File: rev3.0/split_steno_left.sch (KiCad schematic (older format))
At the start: 33 parts, among them J1 USB_B, J2 Audio-Jack-4, P1 TC2030-IDC, SW1 SW_Push, SW10 SW_Push, SW11 SW_Push, SW12 SW_Push, SW13 SW_Push, SW14 SW_Push, SW15 SW_Push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

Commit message: finished routing
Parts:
- added J3: Conn_02x04_Odd_Even, Pin_Headers:Pin_Header_Straight_2x04_Pitch2.54mm, symbol Conn_02x04_Odd_Even
- added J4, J5: Conn_01x03, Pin_Headers:Pin_Header_Straight_1x03_Pitch2.54mm, symbol Conn_01x03
- added J6: Conn_01x02, Pin_Headers:Pin_Header_Straight_1x02_Pitch2.54mm, symbol Conn_01x02
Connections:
- net GND: now also J3.1 (Pin_1), J4.3 (Pin_3), J5.3 (Pin_3), J6.2 (Pin_2)
- net KEY1: now also U2.24 (PD4/OC1A/~SS~)
- net KEY10: now also U2.43 (AC3/ADC3/PA3)
- net KEY11: now also U2.11 (SCLIN/SCL/XCK0/OC0AHS/OC0B/PC1)
- net KEY12: now also U2.10 (SDAIN/SDA/~OC0ALS~/OC0A/PC0)
- net KEY13: now also U2.3 (AC0OUT/AC7/ADC7/PA7)
- net KEY14: now also U2.2 (AC1OUT/AC6/ADC6/PA6)
- net KEY15: now also U2.44 (AC4/ADC4/PA4)
- net KEY16: now also SW19.1, U2.5 (ADC9/PB1)
- net KEY17: now also SW20.1, U2.4 (AREFB/ADC8/PB0); no longer SW19.1
- net KEY18: now also U2.1 (AC5/ADC5/PA5); no longer SW20.1
- net KEY2: now also U2.25 (PD5/OC1B/XCK1/MOSI)
- net KEY3: now also U2.33 (PE3/OC0D/TXD0)
- net KEY4: now also U2.36 (PR0/XTAL2/TOSC2)
- net KEY5: now also U2.42 (AC2/ADC2/PA2)
- net KEY6: now also U2.23 (PD3/OC0D/TXD0)
- net KEY7: now also U2.20 (PD0/OC0A)
- net KEY8: now also U2.32 (PE2/OC0C/RXD0)
- net KEY9: now also U2.41 (AC1/ADC1/PA1)
- net VCC: now also J3.2 (Pin_2), J4.1 (Pin_1), J5.1 (Pin_1)
- net CE: now reaches U2.12 (SDAOUT/RXD0/~OC0BLS~/OC0C/PC2)
- net CE: now also J3.3 (Pin_3)
- net IRQ: now reaches U2.13 (SCLOUT/TXD0/OC0BHS/OC0D/PC3)
- net IRQ: now also J3.8 (Pin_8)
- net CSN: now reaches U2.14 (~SS~/~OC0CLS~/OC1A/PC4)
- net CSN: now also J3.4 (Pin_4)
- net MOSI: now reaches U2.15 (MOSI/XCK1/OC0CHS/OC1B/PC5)
- net MOSI: now also J3.6 (Pin_6)
- net MISO: now reaches U2.16 (CLKRTC/MISO/RXD1/~OC0DLS~/PC6)
- net MISO: now also J3.7 (Pin_7)
- net SCK: now reaches U2.17 (CLKOUT/SCK/TXD1/OC0DHS/PC7)
- net SCK: now also J3.5 (Pin_5)
- net EXTRA1: now reaches U2.22 (PD2/OC0C/RXD0)
- net EXTRA1: now also J5.2 (Pin_2)
- net EXTRA2: now reaches U2.37 (PR1/XTAL1/TOSC1)
- net EXTRA2: now also J6.1 (Pin_1)
- net UNDER_RGB: now reaches U2.6 (DAC0/ADC10/PB2)
- net UNDER_RGB: now also J4.2 (Pin_2)
- no-connect marks 3 -> 6
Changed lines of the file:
@@
 $EndComp
 Text Label 6250 1675 2    60   ~ 0
-KEY17
+KEY16
 $Comp
 L SW_Push SW20
@@
 $EndComp
 Text Label 6250 1900 2    60   ~ 0
-KEY18
+KEY17
 $Comp
 L SW_Push SW1
@@
 	-1   0    0    1
 $EndComp
+$Comp
+L VCC #PWR020
+U 1 1 5AFFE474
+P 7400 2725
+F 0 "#PWR020" H 7400 2575 50  0001 C CNN
+F 1 "VCC" H 7400 2875 50  0000 C CNN
+F 2 "" H 7400 2725 50  0001 C CNN
+F 3 "" H 7400 2725 50  0001 C CNN
+	1    7400 2725
+	1    0    0    -1
+$EndComp
+$Comp
+L VCC #PWR021
+U 1 1 5AFFE4E2
+P 7075 3225
+F 0 "#PWR021" H 7075 3075 50  0001 C CNN
+F 1 "VCC" H 7075 3375 50  0000 C CNN
+F 2 "" H 7075 3225 50  0001 C CNN
+F 3 "" H 7075 3225 50  0001 C CNN
+	1    7075 3225
+	0    1    1    0
+$EndComp
+$Comp
+L Conn_02x04_Odd_Even J3
+U 1 1 5B14A652
+P 5500 2850
+F 0 "J3" H 5550 3050 50  0000 C CNN
+F 1 "Conn_02x04_Odd_Even" H 5550 2550 50  0000 C CNN
+F 2 "Pin_Headers:Pin_Header_Straight_2x04_Pitch2.54mm" H 5500 2850 50  0001 C CNN
+F 3 "" H 5500 2850 50  0001 C CNN
+	1    5500 2850
+	1    0    0    -1
+$EndComp
+Text Label 9775 3775 0    60   ~ 0
+IRQ
+Text Label 9775 3675 0    60   ~ 0
+CE
+Text Label 9775 3875 0    60   ~ 0
+CSN
+Text Label 9775 3975 0    60   ~ 0
+MOSI
+Text Label 9775 4075 0    60   ~ 0
+MISO
+Text Label 9775 4175 0    60   ~ 0
+SCK
 Wire Wire Line
 	8475 1875 8875 1875
@@
 Connection ~ 7400 3025
 Connection ~ 7225 3125
-$Comp
-L VCC #PWR020
-U 1 1 5AFFE474
-P 7400 2725
-F 0 "#PWR020" H 7400 2575 50  0001 C CNN
-F 1 "VCC" H 7400 2875 50  0000 C CNN
-F 2 "" H 7400 2725 50  0001 C CNN
-F 3 "" H 7400 2725 50  0001 C CNN
-	1    7400 2725
-	1    0    0    -1
-$EndComp
-$Comp
-L VCC #PWR021
-U 1 1 5AFFE4E2
-P 7075 3225
-F 0 "#PWR021" H 7075 3075 50  0001 C CNN
-F 1 "VCC" H 7075 3375 50  0000 C CNN
-F 2 "" H 7075 3225 50  0001 C CNN
-F 3 "" H 7075 3225 50  0001 C CNN
-	1    7075 3225
+Wire Wire Line
+	6625 3425 6675 3425
+Wire Wire Line
+	7225 2825 7225 2725
+Wire Wire Line
+	7225 2725 7400 2725
+Text Label 5300 2950 2    60   ~ 0
+SCK
+Text Label 5300 3050 2    60   ~ 0
+MISO
+Text Label 5300 2850 2    60   ~ 0
+CE
+Text Label 5800 2850 0    60   ~ 0
+CSN
+Text Label 5800 2950 0    60   ~ 0
+MOSI
+Text Label 5800 3050 0    60   ~ 0
+IRQ
+$Comp
+L GND #PWR022
+U 1 1 5B14B3CA
+P 5300 2750
+F 0 "#PWR022" H 5300 2500 50  0001 C CNN
+F 1 "GND" H 5300 2600 50  0000 C CNN
+F 2 "" H 5300 2750 50  0001 C CNN
+F 3 "" H 5300 2750 50  0001 C CNN
+	1    5300 2750
+	-1   0    0    1
+$EndComp
+$Comp
+L VCC #PWR023
+U 1 1 5B14B797
+P 5800 2750
+F 0 "#PWR023" H 5800 2600 50  0001 C CNN
+F 1 "VCC" H 5800 2900 50  0000 C CNN
+F 2 "" H 5800 2750 50  0001 C CNN
+F 3 "" H 5800 2750 50  0001 C CNN
+	1    5800 2750
+	1    0    0    -1
+$EndComp
+Text Label 9775 3575 0    60   ~ 0
+KEY11
+Text Label 9775 3475 0    60   ~ 0
+KEY12
+Text Label 9775 2575 0    60   ~ 0
+KEY15
+Text Label 9775 2775 0    60   ~ 0
+KEY14
+Text Label 9775 2875 0    60   ~ 0
+KEY13
+Text Label 9775 2675 0    60   ~ 0
+KEY18
+Text Label 9775 3025 0    60   ~ 0
+KEY17
+Text Label 9775 3125 0    60   ~ 0
+KEY16
+Text Label 9775 3225 0    60   ~ 0
+UNDER_RGB
+Text Label 5775 3525 2    60   ~ 0
+UNDER_RGB
+Text Label 7975 3475 2    60   ~ 0
+KEY7
+Text Label 7975 3775 2    60   ~ 0
+KEY6
+Text Label 7975 3875 2    60   ~ 0
+KEY1
+Text Label 7975 3975 2    60   ~ 0
+KEY2
+Text Label 7975 3325 2    60   ~ 0
+KEY3
+Text Label 7975 2775 2    60   ~ 0
+KEY4
+Text Label 7975 3225 2    60   ~ 0
+KEY8
+Text Label 9775 2275 0    60   ~ 0
+KEY9
+Text Label 9775 2375 0    60   ~ 0
+KEY5
+Text Label 9775 2475 0    60   ~ 0
+KEY10
+Text Label 7975 2875 2    60   ~ 0
+EXTRA2
+Text Label 7975 3675 2    60   ~ 0
+EXTRA1
+NoConn ~ 7975 3575
+NoConn ~ 9775 2175
+NoConn ~ 9775 3325
+Text Label 5775 4100 2    60   ~ 0
+EXTRA1
+Text Label 5775 4500 2    60   ~ 0
+EXTRA2
+$Comp
+L Conn_01x03 J4
+U 1 1 5B15D849
+P 5975 3525
+F 0 "J4" H 5975 3725 50  0000 C CNN
+F 1 "Conn_01x03" H 5975 3325 50  0000 C CNN
+F 2 "Pin_Headers:Pin_Header_Straight_1x03_Pitch2.54mm" H 5975 3525 50  0001 C CNN
+F 3 "" H 5975 3525 50  0001 C CNN
+	1    5975 3525
+	1    0    0    -1
+$EndComp
+$Comp
+L VCC #PWR024
+U 1 1 5B15DA49
+P 5775 3425
+F 0 "#PWR024" H 5775 3275 50  0001 C CNN
+F 1 "VCC" H 5775 3575 50  0000 C CNN
+F 2 "" H 5775 3425 50  0001 C CNN
+F 3 "" H 5775 3425 50  0001 C CNN
+	1    5775 3425
+	1    0    0    -1
+$EndComp
+$Comp
+L GND #PWR025
+U 1 1 5B15DAC3
+P 5775 3625
+F 0 "#PWR025" H 5775 3375 50  0001 C CNN
+F 1 "GND" H 5775 3475 50  0000 C CNN
+F 2 "" H 5775 3625 50  0001 C CNN
+F 3 "" H 5775 3625 50  0001 C CNN
+	1    5775 3625
 	0    1    1    0
 $EndComp
-Wire Wire Line
-	6625 3425 6675 3425
-Wire Wire Line
-	7225 2825 7225 2725
-Wire Wire Line
-	7225 2725 7400 2725
+$Comp
+L Conn_01x03 J5
+U 1 1 5B15DE45
+P 5975 4100
+F 0 "J5" H 5975 4300 50  0000 C CNN
+F 1 "Conn_01x03" H 5975 3900 50  0000 C CNN
+F 2 "Pin_Headers:Pin_Header_Straight_1x03_Pitch2.54mm" H 5975 4100 50  0001 C CNN
+F 3 "" H 5975 4100 50  0001 C CNN
+	1    5975 4100
+	1    0    0    -1
+$EndComp
+$Comp
+L VCC #PWR026
+U 1 1 5B15E01D
+P 5775 4000
+F 0 "#PWR026" H 5775 3850 50  0001 C CNN
+F 1 "VCC" H 5775 4150 50  0000 C CNN
+F 2 "" H 5775 4000 50  0001 C CNN
+F 3 "" H 5775 4000 50  0001 C CNN
+	1    5775 4000
+	1    0    0    -1
+$EndComp
+$Comp
+L GND #PWR027
+U 1 1 5B15E097
+P 5775 4200
+F 0 "#PWR027" H 5775 3950 50  0001 C CNN
+F 1 "GND" H 5775 4050 50  0000 C CNN
+F 2 "" H 5775 4200 50  0001 C CNN
+F 3 "" H 5775 4200 50  0001 C CNN
+	1    5775 4200
+	0    1    1    0
+$EndComp
+$Comp
+L Conn_01x02 J6
+U 1 1 5B15E1F9
+P 5975 4500
+F 0 "J6" H 5975 4600 50  0000 C CNN
+F 1 "Conn_01x02" H 5975 4300 50  0000 C CNN
+F 2 "Pin_Headers:Pin_Header_Straight_1x02_Pitch2.54mm" H 5975 4500 50  0001 C CNN
+F 3 "" H 5975 4500 50  0001 C CNN
+	1    5975 4500
+	1    0    0    -1
+$EndComp
+$Comp
+L GND #PWR028
+U 1 1 5B15E563
+P 5775 4600
+F 0 "#PWR028" H 5775 4350 50  0001 C CNN
+F 1 "GND" H 5775 4450 50  0000 C CNN
+F 2 "" H 5775 4600 50  0001 C CNN
+F 3 "" H 5775 4600 50  0001 C CNN
+	1    5775 4600
+	0    1    1    0
+$EndComp
 $EndSCHEMATC

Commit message: library managed
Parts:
- C1, C2, C3, C4, C5: footprint Capacitors_SMD:C_0603_HandSoldering -> lib_fp:C_0603_HandSoldering
- F1: footprint Fuse_Holders_and_Fuses:Fuse_SMD1206_HandSoldering -> lib_fp:Fuse_SMD1206_HandSoldering
- J1: footprint keyboard_parts:USB_miniB_hirose_5S8 -> lib_fp:USB_miniB_hirose_5S8
- J2: footprint Keebio-Parts:TRRS-PJ-320A -> lib_fp:TRRS-PJ-320A
- J3: footprint Pin_Headers:Pin_Header_Straight_2x04_Pitch2.54mm -> lib_fp:Pin_Header_Straight_2x04_Pitch2.54mm
- J4, J5: footprint Pin_Headers:Pin_Header_Straight_1x03_Pitch2.54mm -> lib_fp:Pin_Header_Straight_1x03_Pitch2.54mm
- J6: footprint Pin_Headers:Pin_Header_Straight_1x02_Pitch2.54mm -> lib_fp:Pin_Header_Straight_1x02_Pitch2.54mm
- P1: footprint Tag-Connect:TC2030-NL_SMALL_AND_IDC_PDI -> lib_fp:TC2030-NL_SMALL_AND_IDC_PDI
- R1, R2: footprint Resistors_SMD:R_0603_HandSoldering -> lib_fp:R_0603_HandSoldering
- SW1, SW10, SW11, SW12, SW13, SW14, SW15, SW16, SW17, SW18, SW2, SW3, SW4, SW5, SW6, SW7, SW8, SW9: footprint MX_Alps_Hybrid:MX-1U-NoLED -> lib_fp:MX-1U-NoLED
- SW19, SW20: footprint MX_Alps_Hybrid:MX-2U-NoLED -> lib_fp:MX-2U-NoLED
- U1: footprint TO_SOT_Packages_SMD:SOT-23-5_HandSoldering -> lib_fp:SOT-23-5_HandSoldering
- U2: footprint Housings_QFP:TQFP-44_10x10mm_Pitch0.8mm -> lib_fp:TQFP-44_10x10mm_Pitch0.8mm
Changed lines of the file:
@@
 F 0 "J1" H 6575 4525 50  0000 L CNN
 F 1 "USB_B" H 6575 4425 50  0000 L CNN
-F 2 "keyboard_parts:USB_miniB_hirose_5S8" H 6925 4025 50  0001 C CNN
+F 2 "lib_fp:USB_miniB_hirose_5S8" H 6925 4025 50  0001 C CNN
 F 3 "" H 6925 4025 50  0001 C CNN
 	1    6775 4075
@@
 F 0 "J2" H 6825 3105 50  0000 C CNN
 F 1 "Audio-Jack-4" H 6995 2655 50  0000 C CNN
-F 2 "Keebio-Parts:TRRS-PJ-320A" H 7125 3125 50  0001 C CNN
+F 2 "lib_fp:TRRS-PJ-320A" H 7125 3125 50  0001 C CNN
 F 3 "" H 7125 3125 50  0001 C CNN
 	1    6875 3025
@@
 F 0 "P1" H 9575 875 40  0000 L CNN
 F 1 "TC2030-IDC" H 9625 1275 40  0000 C CNN
-F 2 "Tag-Connect:TC2030-NL_SMALL_AND_IDC_PDI" H 9625 1075 60  0001 C CNN
+F 2 "lib_fp:TC2030-NL_SMALL_AND_IDC_PDI" H 9625 1075 60  0001 C CNN
 F 3 "" H 9625 1075 60  0001 C CNN
 	1    9625 1075
@@
 F 0 "U1" H 7725 1650 60  0000 C CNN
 F 1 "MIC550X" H 7925 1050 60  0000 C CNN
-F 2 "TO_SOT_Packages_SMD:SOT-23-5_HandSoldering" H 7925 1350 60  0001 C CNN
+F 2 "lib_fp:SOT-23-5_HandSoldering" H 7925 1350 60  0001 C CNN
 F 3 "" H 7925 1350 60  0001 C CNN
 	1    7925 1350
@@
 F 0 "U2" H 8125 4375 50  0000 L BNN
 F 1 "ATXMEGA-A4U-EPAD" H 9075 1925 50  0000 L BNN
-F 2 "Housings_QFP:TQFP-44_10x10mm_Pitch0.8mm" H 8875 3175 50  0001 C CIN
+F 2 "lib_fp:TQFP-44_10x10mm_Pitch0.8mm" H 8875 3175 50  0001 C CIN
 F 3 "" H 8875 3175 50  0001 C CNN
 	1    8875 3175
@@
 F 0 "C1" H 8525 1450 50  0000 L CNN
 F 1 "10uF" H 8525 1250 50  0000 L CNN
-F 2 "Capacitors_SMD:C_0603_HandSoldering" H 8538 1200 50  0001 C CNN
+F 2 "lib_fp:C_0603_HandSoldering" H 8538 1200 50  0001 C CNN
 F 3 "" H 8500 1350 50  0001 C CNN
 	1    8500 1350
@@
 F 0 "C2" H 9100 1725 50  0000 L CNN
 F 1 "0.1uF" H 9100 1525 50  0000 L CNN
-F 2 "Capacitors_SMD:C_0603_HandSoldering" H 9113 1475 50  0001 C CNN
+F 2 "lib_fp:C_0603_HandSoldering" H 9113 1475 50  0001 C CNN
 F 3 "" H 9075 1625 50  0001 C CNN
 	1    9075 1625
@@
 F 0 "C3" H 9350 1725 50  0000 L CNN
 F 1 "0.1uF" H 9350 1525 50  0000 L CNN
-F 2 "Capacitors_SMD:C_0603_HandSoldering" H 9363 1475 50  0001 C CNN
+F 2 "lib_fp:C_0603_HandSoldering" H 9363 1475 50  0001 C CNN
 F 3 "" H 9325 1625 50  0001 C CNN
 	1    9325 1625
@@
 F 0 "C4" H 9600 1725 50  0000 L CNN
 F 1 "0.1uF" H 9600 1525 50  0000 L CNN
-F 2 "Capacitors_SMD:C_0603_HandSoldering" H 9613 1475 50  0001 C CNN
+F 2 "lib_fp:C_0603_HandSoldering" H 9613 1475 50  0001 C CNN
 F 3 "" H 9575 1625 50  0001 C CNN
 	1    9575 1625
@@
 F 0 "C5" H 9850 1725 50  0000 L CNN
 F 1 "0.1uF" H 9850 1525 50  0000 L CNN
-F 2 "Capacitors_SMD:C_0603_HandSoldering" H 9863 1475 50  0001 C CNN
+F 2 "lib_fp:C_0603_HandSoldering" H 9863 1475 50  0001 C CNN
 F 3 "" H 9825 1625 50  0001 C CNN
 	1    9825 1625
@@
 F 0 "SW5" H 4275 1325 50  0000 L CNN
 F 1 "SW_Push" H 4225 1165 50  0001 C CNN
-F 2 "MX_Alps_Hybrid:MX-1U-NoLED" H 4225 1425 50  0001 C CNN
+F 2 "lib_fp:MX-1U-NoLED" H 4225 1425 50  0001 C CNN
 F 3 "" H 4225 1425 50  0001 C CNN
 	1    4225 1225
@@
 F 0 "F1" V 7305 3875 50  0000 C CNN
 F 1 "Fuse" V 7150 3875 50  0000 C CNN
-F 2 "Fuse_Holders_and_Fuses:Fuse_SMD1206_HandSoldering" V 7155 3875 50  0001 C CNN
+F 2 "lib_fp:Fuse_SMD1206_HandSoldering" V 7155 3875 50  0001 C CNN
 F 3 "" H 7225 3875 50  0001 C CNN
 	1    7225 3875
@@
 F 0 "SW6" H 4275 1550 50  0000 L CNN
 F 1 "SW_Push" H 4225 1390 50  0001 C CNN
-F 2 "MX_Alps_Hybrid:MX-1U-NoLED" H 4225 1650 50  0001 C CNN
+F 2 "lib_fp:MX-1U-NoLED" H 4225 1650 50  0001 C CNN
 F 3 "" H 4225 1650 50  0001 C CNN
 	1    4225 1450
@@
 F 0 "SW7" H 4275 1775 50  0000 L CNN
 F 1 "SW_Push" H 4225 1615 50  0001 C CNN
-F 2 "MX_Alps_Hybrid:MX-1U-NoLED" H 4225 1875 50  0001 C CNN
+F 2 "lib_fp:MX-1U-NoLED" H 4225 1875 50  0001 C CNN
 F 3 "" H 4225 1875 50  0001 C CNN
 	1    4225 1675
@@
 F 0 "SW8" H 4275 2000 50  0000 L CNN
 F 1 "SW_Push" H 4225 1840 50  0001 C CNN
-F 2 "MX_Alps_Hybrid:MX-1U-NoLED" H 4225 2100 50  0001 C CNN
+F 2 "lib_fp:MX-1U-NoLED" H 4225 2100 50  0001 C CNN
 F 3 "" H 4225 2100 50  0001 C CNN
 	1    4225 1900
@@
 F 0 "SW9" H 5025 1325 50  0000 L CNN
 F 1 "SW_Push" H 4975 1165 50  0001 C CNN
-F 2 "MX_Alps_Hybrid:MX-1U-NoLED" H 4975 1425 50  0001 C CNN
+F 2 "lib_fp:MX-1U-NoLED" H 4975 1425 50  0001 C CNN
 F 3 "" H 4975 1425 50  0001 C CNN
 	1    4975 1225
@@
 F 0 "SW10" H 5025 1550 50  0000 L CNN
 F 1 "SW_Push" H 4975 1390 50  0001 C CNN
-F 2 "MX_Alps_Hybrid:MX-1U-NoLED" H 4975 1650 50  0001 C CNN
+F 2 "lib_fp:MX-1U-NoLED" H 4975 1650 50  0001 C CNN
 F 3 "" H 4975 1650 50  0001 C CNN
 	1    4975 1450
@@
 F 0 "SW11" H 5025 1775 50  0000 L CNN
 F 1 "SW_Push" H 4975 1615 50  0001 C CNN
-F 2 "MX_Alps_Hybrid:MX-1U-NoLED" H 4975 1875 50  0001 C CNN
+F 2 "lib_fp:MX-1U-NoLED" H 4975 1875 50  0001 C CNN
 F 3 "" H 4975 1875 50  0001 C CNN
 	1    4975 1675
@@
 F 0 "SW12" H 5025 2000 50  0000 L CNN
 F 1 "SW_Push" H 4975 1840 50  0001 C CNN
-F 2 "MX_Alps_Hybrid:MX-1U-NoLED" H 4975 2100 50  0001 C CNN
+F 2 "lib_fp:MX-1U-NoLED" H 4975 2100 50  0001 C CNN
 F 3 "" H 4975 2100 50  0001 C CNN
 	1    4975 1900
@@
 F 0 "SW13" H 5750 1325 50  0000 L CNN
 F 1 "SW_Push" H 5700 1165 50  0001 C CNN
-F 2 "MX_Alps_Hybrid:MX-1U-NoLED" H 5700 1425 50  0001 C CNN
+F 2 "lib_fp:MX-1U-NoLED" H 5700 1425 50  0001 C CNN
 F 3 "" H 5700 1425 50  0001 C CNN
 	1    5700 1225
@@
 F 0 "SW14" H 5750 1550 50  0000 L CNN
 F 1 "SW_Push" H 5700 1390 50  0001 C CNN
-F 2 "MX_Alps_Hybrid:MX-1U-NoLED" H 5700 1650 50  0001 C CNN
+F 2 "lib_fp:MX-1U-NoLED" H 5700 1650 50  0001 C CNN
 F 3 "" H 5700 1650 50  0001 C CNN
 	1    5700 1450
@@
 F 0 "SW15" H 5750 1775 50  0000 L CNN
 F 1 "SW_Push" H 5700 1615 50  0001 C CNN
-F 2 "MX_Alps_Hybrid:MX-1U-NoLED" H 5700 1875 50  0001 C CNN
+F 2 "lib_fp:MX-1U-NoLED" H 5700 1875 50  0001 C CNN
 F 3 "" H 5700 1875 50  0001 C CNN
 	1    5700 1675
@@
 F 0 "SW16" H 5750 2000 50  0000 L CNN
 F 1 "SW_Push" H 5700 1840 50  0001 C CNN
-F 2 "MX_Alps_Hybrid:MX-1U-NoLED" H 5700 2100 50  0001 C CNN
+F 2 "lib_fp:MX-1U-NoLED" H 5700 2100 50  0001 C CNN
 F 3 "" H 5700 2100 50  0001 C CNN
 	1    5700 1900
@@
 F 0 "SW17" H 6500 1325 50  0000 L CNN
 F 1 "SW_Push" H 6450 1165 50  0001 C CNN
-F 2 "MX_Alps_Hybrid:MX-1U-NoLED" H 6450 1425 50  0001 C CNN
+F 2 "lib_fp:MX-1U-NoLED" H 6450 1425 50  0001 C CNN
 F 3 "" H 6450 1425 50  0001 C CNN
 	1    6450 1225
@@
 F 0 "SW18" H 6500 1550 50  0000 L CNN
 F 1 "SW_Push" H 6450 1390 50  0001 C CNN
-F 2 "MX_Alps_Hybrid:MX-1U-NoLED" H 6450 1650 50  0001 C CNN
+F 2 "lib_fp:MX-1U-NoLED" H 6450 1650 50  0001 C CNN
 F 3 "" H 6450 1650 50  0001 C CNN
 	1    6450 1450
@@
 F 0 "SW19" H 6500 1775 50  0000 L CNN
 F 1 "SW_Push" H 6450 1615 50  0001 C CNN
-F 2 "MX_Alps_Hybrid:MX-2U-NoLED" H 6450 1875 50  0001 C CNN
+F 2 "lib_fp:MX-2U-NoLED" H 6450 1875 50  0001 C CNN
 F 3 "" H 6450 1875 50  0001 C CNN
 	1    6450 1675
@@
 F 0 "SW20" H 6500 2000 50  0000 L CNN
 F 1 "SW_Push" H 6450 1840 50  0001 C CNN
-F 2 "MX_Alps_Hybrid:MX-2U-NoLED" H 6450 2100 50  0001 C CNN
+F 2 "lib_fp:MX-2U-NoLED" H 6450 2100 50  0001 C CNN
 F 3 "" H 6450 2100 50  0001 C CNN
 	1    6450 1900
@@
 F 0 "SW1" H 3550 1325 50  0000 L CNN
 F 1 "SW_Push" H 3500 1165 50  0001 C CNN
-F 2 "MX_Alps_Hybrid:MX-1U-NoLED" H 3500 1425 50  0001 C CNN
+F 2 "lib_fp:MX-1U-NoLED" H 3500 1425 50  0001 C CNN
 F 3 "" H 3500 1425 50  0001 C CNN
 	1    3500 1225
@@
 F 0 "SW2" H 3550 1550 50  0000 L CNN
 F 1 "SW_Push" H 3500 1390 50  0001 C CNN
-F 2 "MX_Alps_Hybrid:MX-1U-NoLED" H 3500 1650 50  0001 C CNN
+F 2 "lib_fp:MX-1U-NoLED" H 3500 1650 50  0001 C CNN
 F 3 "" H 3500 1650 50  0001 C CNN
 	1    3500 1450
@@
 F 0 "SW3" H 3550 1775 50  0000 L CNN
 F 1 "SW_Push" H 3500 1615 50  0001 C CNN
-F 2 "MX_Alps_Hybrid:MX-1U-NoLED" H 3500 1875 50  0001 C CNN
+F 2 "lib_fp:MX-1U-NoLED" H 3500 1875 50  0001 C CNN
 F 3 "" H 3500 1875 50  0001 C CNN
 	1    3500 1675
@@
 F 0 "SW4" H 3550 2000 50  0000 L CNN
 F 1 "SW_Push" H 3500 1840 50  0001 C CNN
-F 2 "MX_Alps_Hybrid:MX-1U-NoLED" H 3500 2100 50  0001 C CNN
+F 2 "lib_fp:MX-1U-NoLED" H 3500 2100 50  0001 C CNN
 F 3 "" H 3500 2100 50  0001 C CNN
 	1    3500 1900
@@
 F 0 "R1" V 7305 2975 50  0000 C CNN
 F 1 "4.7k" V 7225 2975 50  0000 C CNN
-F 2 "Resistors_SMD:R_0603_HandSoldering" V 7155 2975 50  0001 C CNN
+F 2 "lib_fp:R_0603_HandSoldering" V 7155 2975 50  0001 C CNN
 F 3 "" H 7225 2975 50  0001 C CNN
 	1    7225 2975
@@
 F 0 "R2" V 7480 2875 50  0000 C CNN
 F 1 "4.7k" V 7400 2875 50  0000 C CNN
-F 2 "Resistors_SMD:R_0603_HandSoldering" V 7330 2875 50  0001 C CNN
+F 2 "lib_fp:R_0603_HandSoldering" V 7330 2875 50  0001 C CNN
 F 3 "" H 7400 2875 50  0001 C CNN
 	1    7400 2875
@@
 F 0 "J3" H 5550 3050 50  0000 C CNN
 F 1 "Conn_02x04_Odd_Even" H 5550 2550 50  0000 C CNN
-F 2 "Pin_Headers:Pin_Header_Straight_2x04_Pitch2.54mm" H 5500 2850 50  0001 C CNN
+F 2 "lib_fp:Pin_Header_Straight_2x04_Pitch2.54mm" H 5500 2850 50  0001 C CNN
 F 3 "" H 5500 2850 50  0001 C CNN
 	1    5500 2850
@@
 F 0 "J4" H 5975 3725 50  0000 C CNN
 F 1 "Conn_01x03" H 5975 3325 50  0000 C CNN
-F 2 "Pin_Headers:Pin_Header_Straight_1x03_Pitch2.54mm" H 5975 3525 50  0001 C CNN
+F 2 "lib_fp:Pin_Header_Straight_1x03_Pitch2.54mm" H 5975 3525 50  0001 C CNN
 F 3 "" H 5975 3525 50  0001 C CNN
 	1    5975 3525
@@
 F 0 "J5" H 5975 4300 50  0000 C CNN
 F 1 "Conn_01x03" H 5975 3900 50  0000 C CNN
-F 2 "Pin_Headers:Pin_Header_Straight_1x03_Pitch2.54mm" H 5975 4100 50  0001 C CNN
+F 2 "lib_fp:Pin_Header_Straight_1x03_Pitch2.54mm" H 5975 4100 50  0001 C CNN
 F 3 "" H 5975 4100 50  0001 C CNN
 	1    5975 4100
@@
 F 0 "J6" H 5975 4600 50  0000 C CNN
 F 1 "Conn_01x02" H 5975 4300 50  0000 C CNN
-F 2 "Pin_Headers:Pin_Header_Straight_1x02_Pitch2.54mm" H 5975 4500 50  0001 C CNN
+F 2 "lib_fp:Pin_Header_Straight_1x02_Pitch2.54mm" H 5975 4500 50  0001 C CNN
 F 3 "" H 5975 4500 50  0001 C CNN
 	1    5975 4500

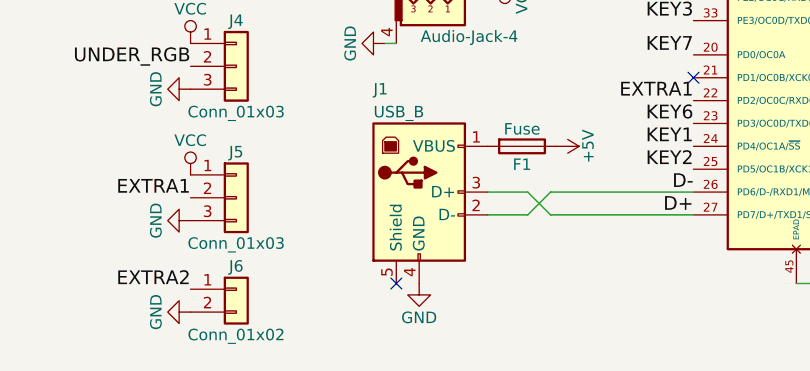
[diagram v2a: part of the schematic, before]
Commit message: filled gnd plane on left
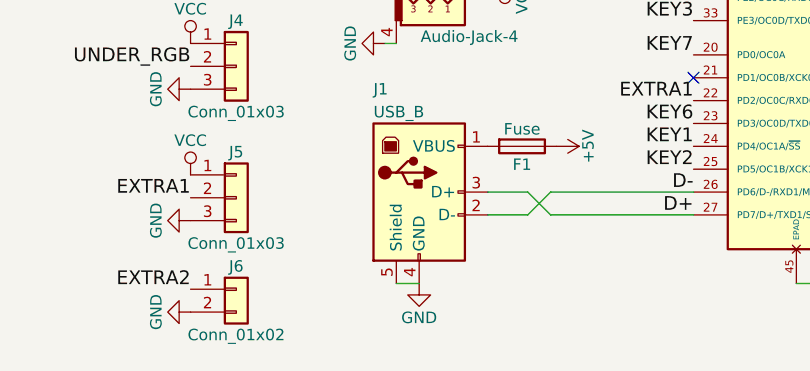
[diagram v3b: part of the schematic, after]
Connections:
- net GND: now also J1.5 (Shield)
- no-connect marks 6 -> 5
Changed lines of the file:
@@
 EESchema Schematic File Version 2
-LIBS:atmel
-LIBS:bus_switches
-LIBS:conn_usb
-LIBS:kicad_util
-LIBS:logic
-LIBS:microchip
-LIBS:nordic
-LIBS:nordic2
-LIBS:onsemi
-LIBS:rgb_led
-LIBS:silabs
-LIBS:switch
-LIBS:Tag-Connect
-LIBS:power
-LIBS:device
-LIBS:switches
-LIBS:relays
-LIBS:motors
-LIBS:transistors
-LIBS:conn
-LIBS:linear
-LIBS:regul
-LIBS:74xx
-LIBS:cmos4000
-LIBS:adc-dac
-LIBS:memory
-LIBS:xilinx
-LIBS:microcontrollers
-LIBS:dsp
-LIBS:analog_switches
-LIBS:motorola
-LIBS:texas
-LIBS:intel
-LIBS:audio
-LIBS:interface
-LIBS:digital-audio
-LIBS:philips
-LIBS:display
-LIBS:cypress
-LIBS:siliconi
-LIBS:opto
-LIBS:contrib
-LIBS:valves
-LIBS:split_steno_left-cache
+LIBS:split_steno_left
 EELAYER 25 0
 EELAYER END
@@
 Text Label 7975 4075 2    60   ~ 0
 D-
-NoConn ~ 6675 4475
 $Comp
 L Fuse F1
@@
 	0    1    1    0
 $EndComp
+Wire Wire Line
+	6675 4475 6775 4475
 $EndSCHEMATC
